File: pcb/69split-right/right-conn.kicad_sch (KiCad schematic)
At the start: 1 part, among them J3 USB_C_Receptacle

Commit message: Moved things around so it's less confusing.
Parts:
- removed J3: USB_C_Receptacle, Connector_USB:USB_C_Receptacle_Amphenol_12401548E4-2A, symbol Connector:USB_C_Receptacle
- added J1: USB_C_Receptacle, Connector_USB:USB_C_Receptacle_Amphenol_12401548E4-2A, symbol Connector:USB_C_Receptacle
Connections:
- net COL10: now also J1.A3 (TX1-)
- net COL11: now also J1.A2 (TX1+)
- net COL12: now also J1.A10 (RX2-)
- net COL13: now also J1.A11 (RX2+)
- net COL14: now also J1.B3 (TX2-)
- net COL6: now also J1.A6 (D+)
- net COL7: now also J1.B6 (D+)
- net COL8: now also J1.B10 (RX1-)
- net COL9: now also J1.B11 (RX1+)
- net GND: now also J1.A1 (GND), J1.A12 (GND), J1.B1 (GND), J1.B12 (GND), J1.S1 (SHIELD)
- net GPIO_OUT_PB5: now also J1.B8 (SBU2)
- net GPIO_OUT_PB6: now also J1.A8 (SBU1)
- net GPIO_OUT_PB7: now also J1.B2 (TX2+)
- net ROW0: now also J1.A4 (VBUS), J1.A9 (VBUS), J1.B4 (VBUS), J1.B9 (VBUS)
- net ROW1: now also J1.A5 (CC1)
- net ROW2: now also J1.B5 (CC2)
- net ROW3: now also J1.A7 (D-)
- net ROW4: now also J1.B7 (D-)
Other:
- note added: "RIGHT KEYBOARD CONNECTOR"
- note removed: "LEFT KEYBOARD CONNECTOR"

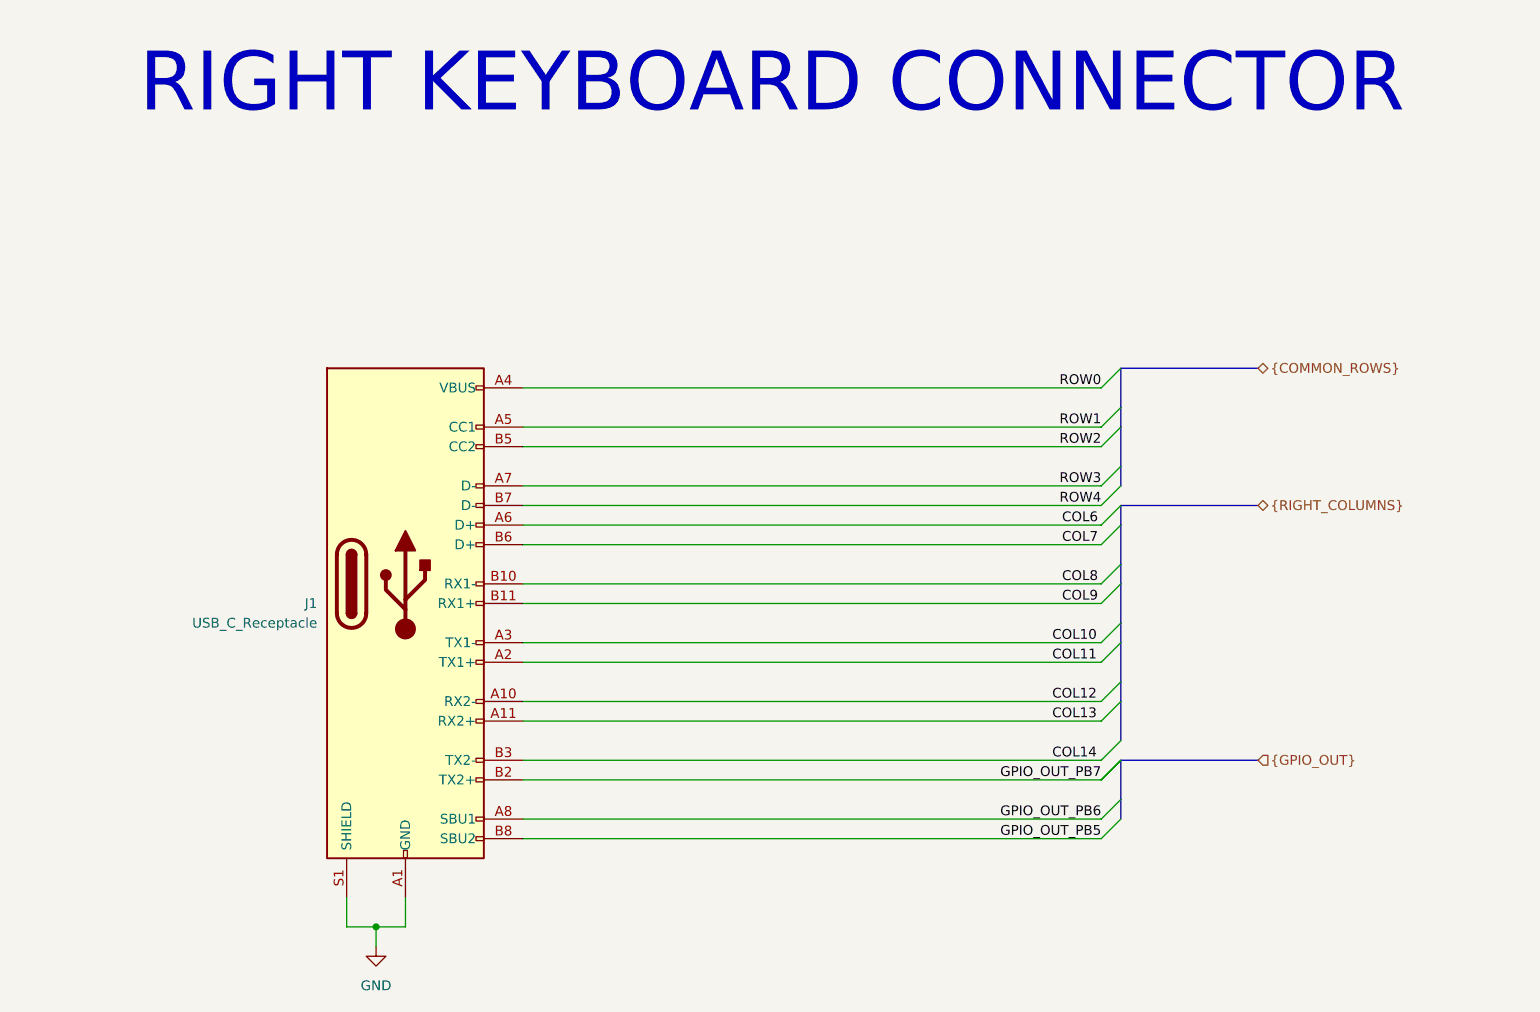
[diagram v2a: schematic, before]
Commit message: Started changing things gain to use an I/O expander with I2C.
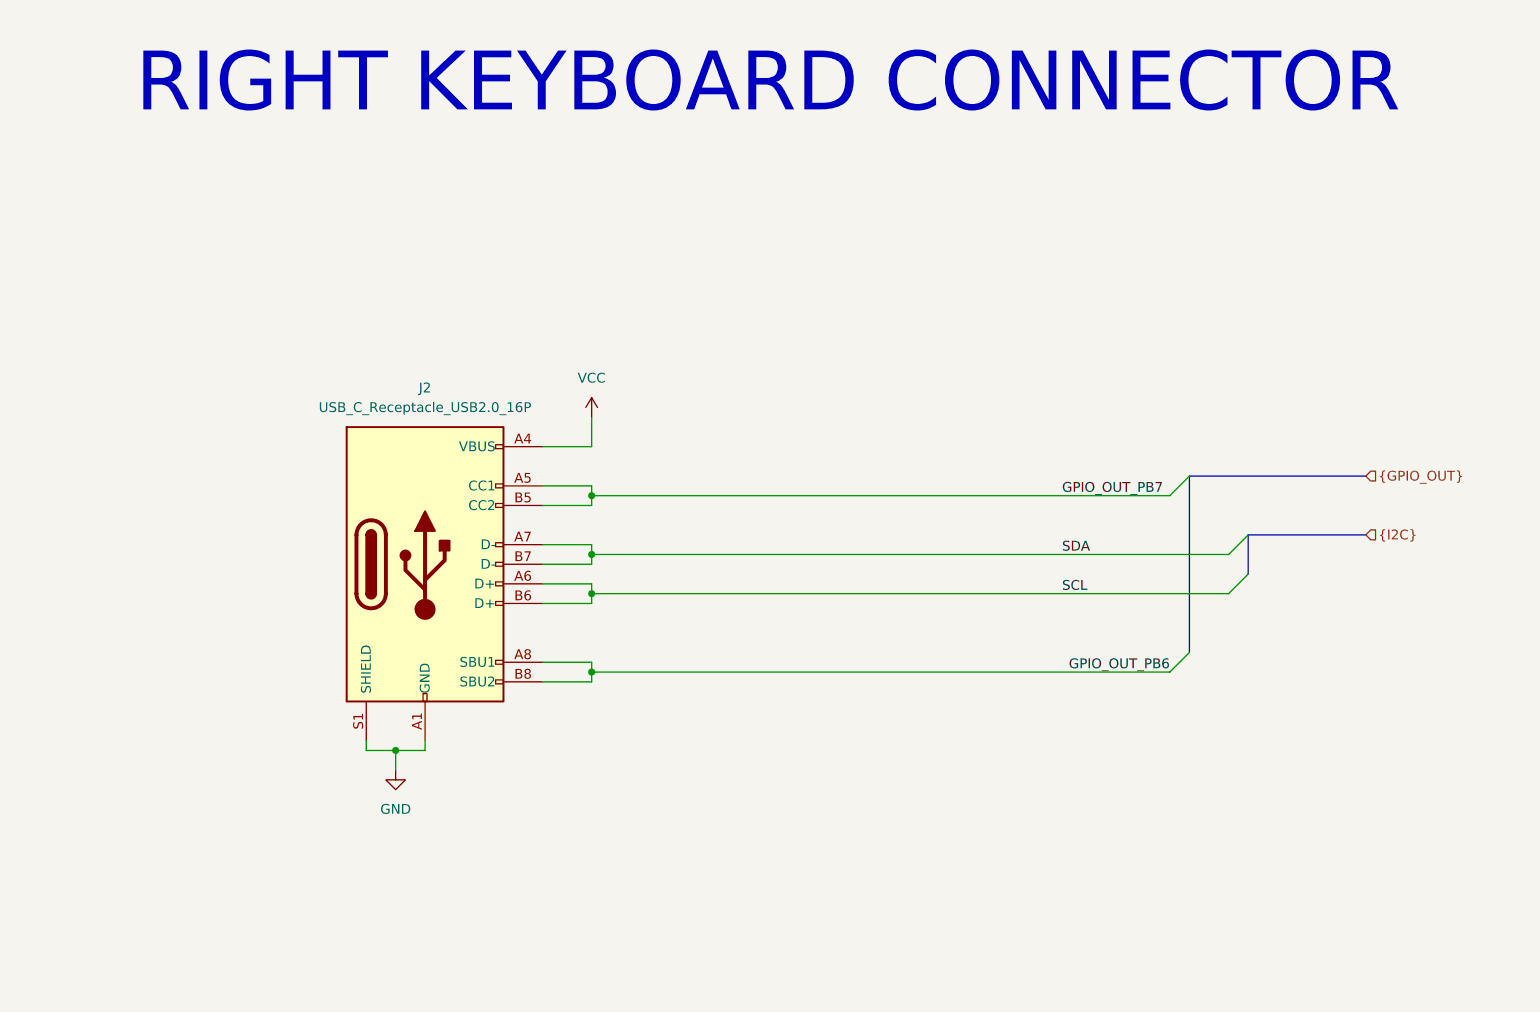
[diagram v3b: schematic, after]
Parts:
- removed J1: USB_C_Receptacle, Connector_USB:USB_C_Receptacle_Amphenol_12401548E4-2A, symbol Connector:USB_C_Receptacle
- added J2: USB_C_Receptacle_USB2.0_16P, Connector_USB:USB_C_Receptacle_JAE_DX07S016JA1R1500, symbol Connector:USB_C_Receptacle_USB2.0_16P
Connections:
- net GND: now also J2.A1 (GND), J2.A12 (GND), J2.B1 (GND), J2.B12 (GND), J2.S1 (SHIELD)
- net GPIO_OUT_PB6: now also J2.A8 (SBU1), J2.B8 (SBU2)
- net GPIO_OUT_PB7: now also J2.A5 (CC1), J2.B5 (CC2)
- new net SCL: J2.A6 (D+), J2.B6 (D+)
- new net SDA: J2.A7 (D-), J2.B7 (D-)
- new net VCC: J2.A4 (VBUS), J2.A9 (VBUS), J2.B4 (VBUS), J2.B9 (VBUS)
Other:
- company: (none) -> Yiannis Michael
- title: 69SPLIT KEYBOARD -> 69SPLIT

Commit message: First draft of the right side.
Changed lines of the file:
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@@
+	)
+	(junction
+		(at 125.73 86.36)
+		(diameter 0)
+		(color 0 0 0 0)
 	)
 	(junction
@@
 					(unit 1)
 				)
+			)
+		)
+	)
+	(symbol
+		(lib_id "power:PWR_FLAG")
+		(at 125.73 86.36 270)
+		(unit 1)
+		(exclude_from_sim no)
+		(in_bom yes)
+		(on_board yes)
+		(dnp no)
+		(fields_autoplaced yes)
+		(property "Reference" "#FLG01"
+			(at 127.635 86.36 0)
+			(effects
+				(font
+					(size 1.27 1.27)
+				)
+				(hide yes)
+			)
+		)
+		(property "Value" "PWR_FLAG"
+			(at 129.54 86.3599 90)
+			(effects
+				(font
+					(size 1.27 1.27)
+				)
+				(justify left)
+			)
+		)
+		(property "Footprint" ""
+			(at 125.73 86.36 0)
+			(effects
+				(font
+					(size 1.27 1.27)
+				)
+				(hide yes)
+			)
+		)
+		(property "Datasheet" "~"
+			(at 125.73 86.36 0)
+			(effects
+				(font
+					(size 1.27 1.27)
+				)
+				(hide yes)
+			)
+		)
+		(property "Description" "Special symbol for telling ERC where power comes from"
+			(at 125.73 86.36 0)
+			(effects
+				(font
+					(size 1.27 1.27)
+				)
+				(hide yes)
+			)
+		)
+		(pin "1"
+		)
+		(instances
+			(project ""
+				(path "/f79c3bfa-40a7-4d04-ac4b-e56fce3d0867/e52f6576-264c-459a-9037-dc2e10a35447"
+					(reference "#FLG01")
+					(unit 1)
+				)

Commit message: I think the right side is done???. Added image and 3D files.
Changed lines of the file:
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@@
 	)
 	(bus_entry
-		(at 208.28 100.33)
+		(at 213.36 100.33)
 		(size 2.54 -2.54)
 		(stroke
@@
 	)
 	(bus_entry
-		(at 208.28 105.41)
+		(at 213.36 105.41)
 		(size 2.54 -2.54)
 		(stroke
@@
 	(bus
 		(pts
-			(xy 203.2 90.17) (xy 226.06 90.17)
+			(xy 203.2 90.17) (xy 231.14 90.17)
 		)
 		(stroke
@@
 	(bus
 		(pts
-			(xy 210.82 97.79) (xy 210.82 102.87)
+			(xy 215.9 97.79) (xy 215.9 102.87)
 		)
 		(stroke
@@
 	(wire
 		(pts
-			(xy 125.73 100.33) (xy 208.28 100.33)
+			(xy 125.73 100.33) (xy 213.36 100.33)
 		)
 		(stroke
@@
 	(wire
 		(pts
-			(xy 125.73 105.41) (xy 208.28 105.41)
+			(xy 125.73 105.41) (xy 213.36 105.41)
 		)
 		(stroke
@@
 	(bus
 		(pts
-			(xy 210.82 97.79) (xy 226.06 97.79)
+			(xy 215.9 97.79) (xy 231.14 97.79)
 		)
 		(stroke
@@
 	)
 	(label "SDA"
-		(at 186.69 100.33 0)
+		(at 208.28 100.33 0)
 		(effects
 			(font
@@
 	)
 	(label "SCL"
-		(at 186.69 105.41 0)
+		(at 208.28 105.41 0)
 		(effects
 			(font
@@
 	(hierarchical_label "{GPIO_OUT}"
 		(shape input)
-		(at 226.06 90.17 0)
+		(at 231.14 90.17 0)
 		(effects
 			(font
@@
 	(hierarchical_label "{I2C}"
 		(shape input)
-		(at 226.06 97.79 0)
-		(effects
-			(font
+		(at 231.14 97.79 0)
+		(effects
+			(font

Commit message: Final touches.
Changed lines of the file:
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@@
 		(title "69SPLIT")
 		(date "2025-07-28")
-		(rev "1")
+		(rev "A")
 		(company "Yiannis Michael")
 		(comment 1 "Yiannis Michael")
@@
 	)
 	(hierarchical_label "{GPIO_OUT}"
-		(shape input)
+		(shape output)
 		(at 231.14 90.17 0)
 		(effects
@@
 	)
 	(hierarchical_label "{I2C}"
-		(shape input)
+		(shape bidirectional)
 		(at 231.14 97.79 0)
 		(effects
